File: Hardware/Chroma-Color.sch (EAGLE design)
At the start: 65 parts, among them J1 15-91-1102, J2 87832-6422, J3 1775470-6, J4 D2514-6V0C-AR-WD, J7 26-64-4040, U1 EP4CE6E22C8N, U2 ADP3338AKCZ-3.3-RL, U3 ADP3338AKCZ-2.5-RL, U4 NCV565ST12T3G, U5 M25P40-VMN6TPBCT, X1 ASDMB-50.000MHZ-LC-T

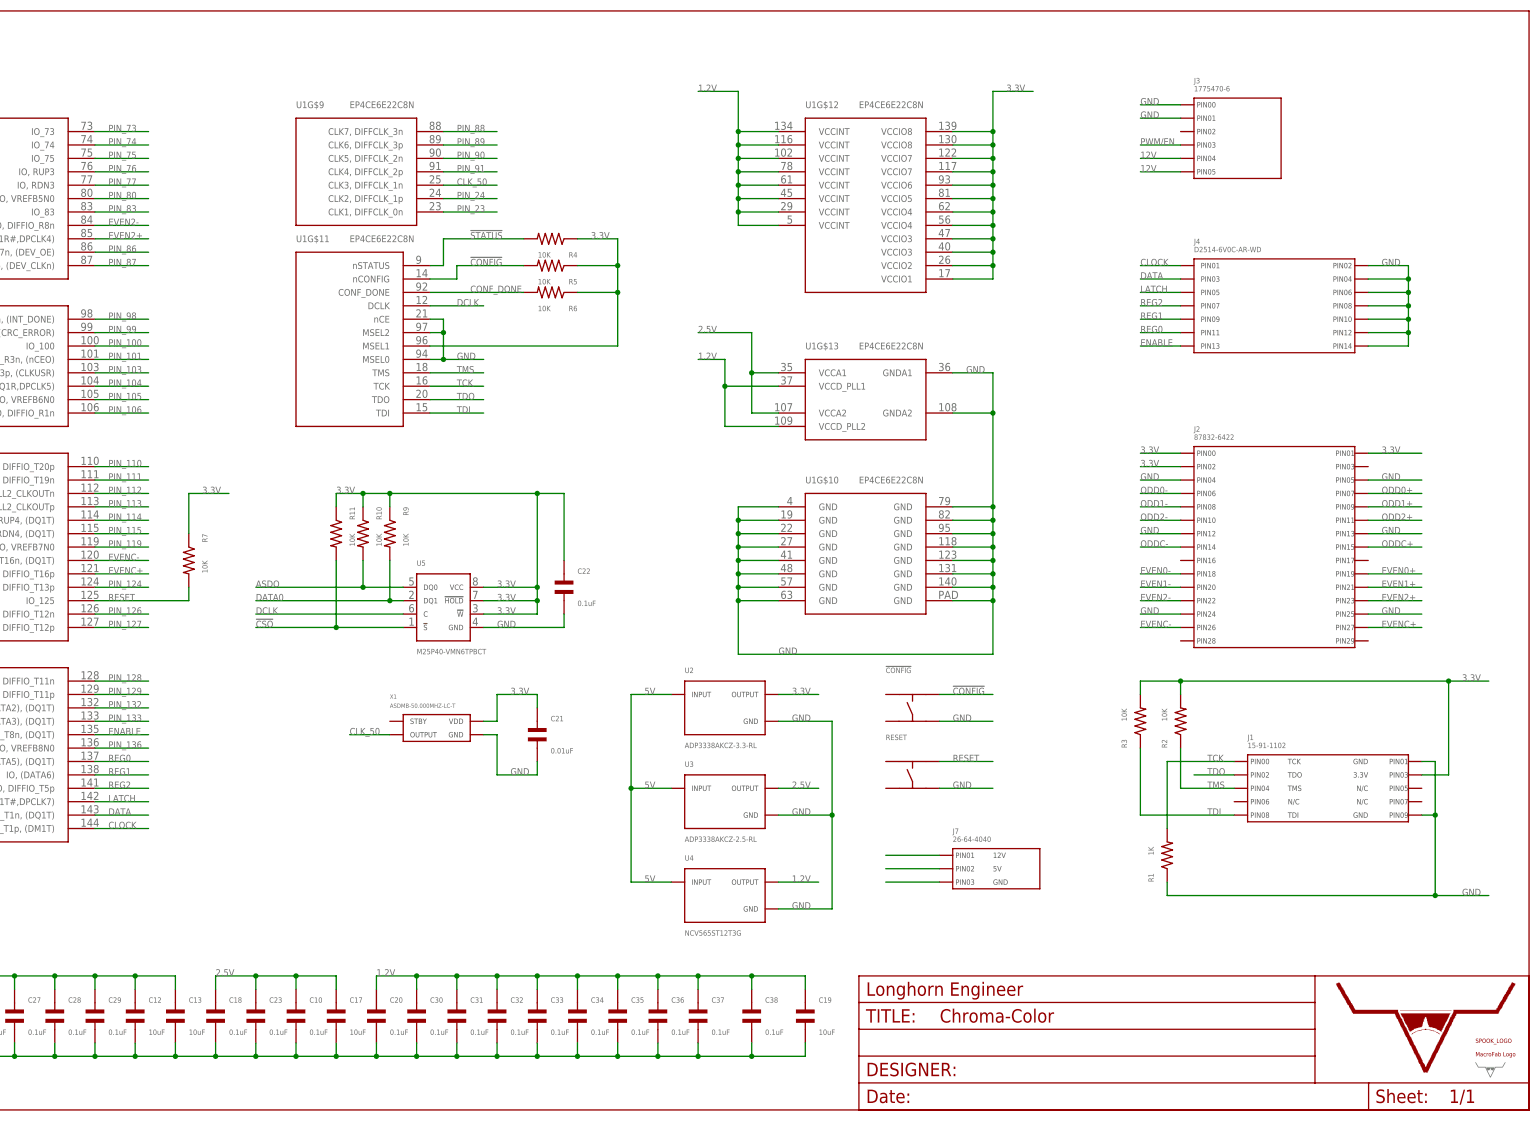
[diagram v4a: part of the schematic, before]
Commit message: Silkscreen done. Added 2SW and 2LED.
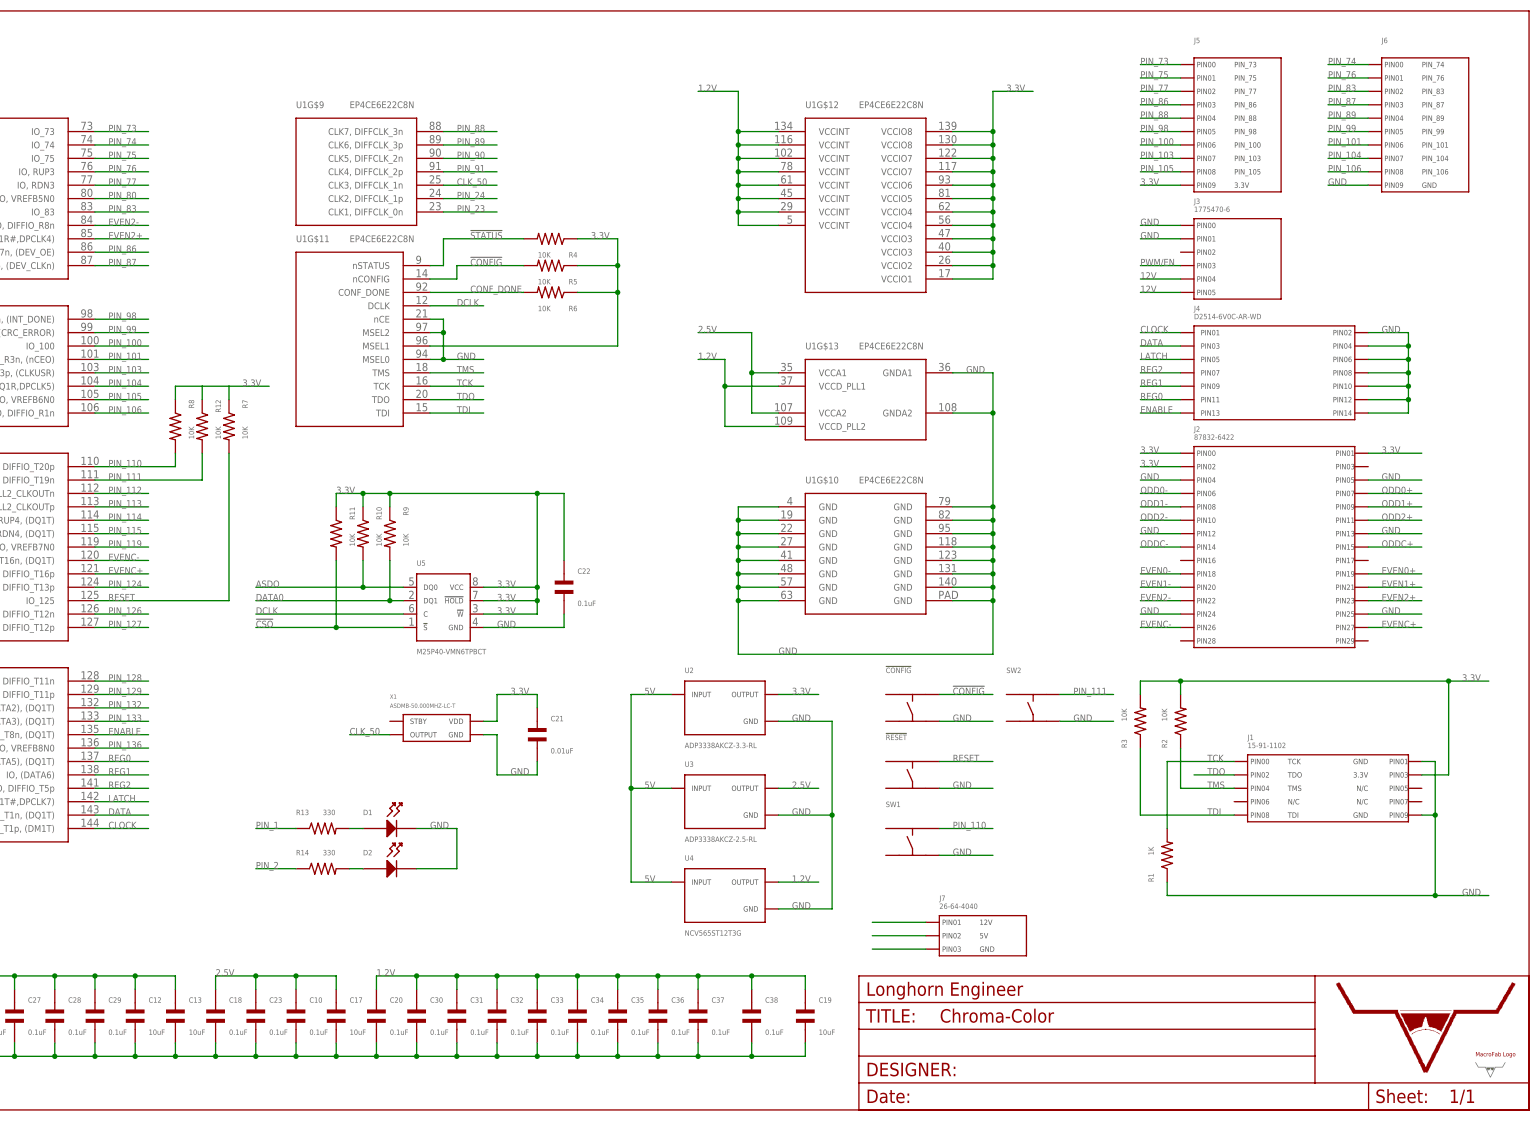
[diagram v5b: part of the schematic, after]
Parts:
- removed LOGO1: SPOOKY_LOGOSPOOKY_LOGO, PP_Aesthetics:SPOOKY_LOGOSPOOKY_LOGO
- added D1, D2: (no value), MF_LEDs:LED_SINGLE_0805
- added J5, J6: (no value), MF_Connectors:HEADER_01X10_PTH_2.54MM
- added R12, R8: 10K, MF_Passives:RESISTOR_0603
- added R13, R14: 330, MF_Passives:RESISTOR_0603
- added SW1, SW2: (no value), MF_Switches:TACT_4.2MM
- R1, R10, R11, R2, R3, R4, R5, R6, R7, R9: device MF_Passives:RESISTOR_0805 -> MF_Passives:RESISTOR_0603
- U$2: value MF_LOGOLOGO_TEXT -> MF_LOGOLOGO_MEDIUM; device PP_Aesthetics:MF_LOGOLOGO_TEXT -> PP_Aesthetics:MF_LOGOLOGO_MEDIUM
- renumbered RESET to !RESET
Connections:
- new net N$1: D1.ANODE, R13.P$2
- new net N$2: D2.ANODE, R14.P$2
- net 3.3V: now also J5.PIN9, R12.P$1, R8.P$1
- net GND: now also D1.CATHODE, D2.CATHODE, J6.PIN9, SW1.P$4, SW2.P$4
- net PIN_1: now also R13.P$1
- net PIN_100: now also J5.PIN6
- net PIN_101: now also J6.PIN6
- net PIN_103: now also J5.PIN7
- net PIN_104: now also J6.PIN7
- net PIN_105: now also J5.PIN8
- net PIN_106: now also J6.PIN8
- net PIN_110: now also R8.P$2, SW1.P$2
- net PIN_111: now also R12.P$2, SW2.P$2
- net PIN_2: now also R14.P$1
- net PIN_73: now also J5.PIN0
- net PIN_74: now also J6.PIN0
- net PIN_75: now also J5.PIN1
- net PIN_76: now also J6.PIN1
- net PIN_77: now also J5.PIN2
- net PIN_83: now also J6.PIN2
- net PIN_86: now also J5.PIN3
- net PIN_87: now also J6.PIN3
- net PIN_88: now also J5.PIN4
- net PIN_89: now also J6.PIN4
- net PIN_98: now also J5.PIN5
- net PIN_99: now also J6.PIN5
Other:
- moved on the sheet: J3, J4, J7, R7

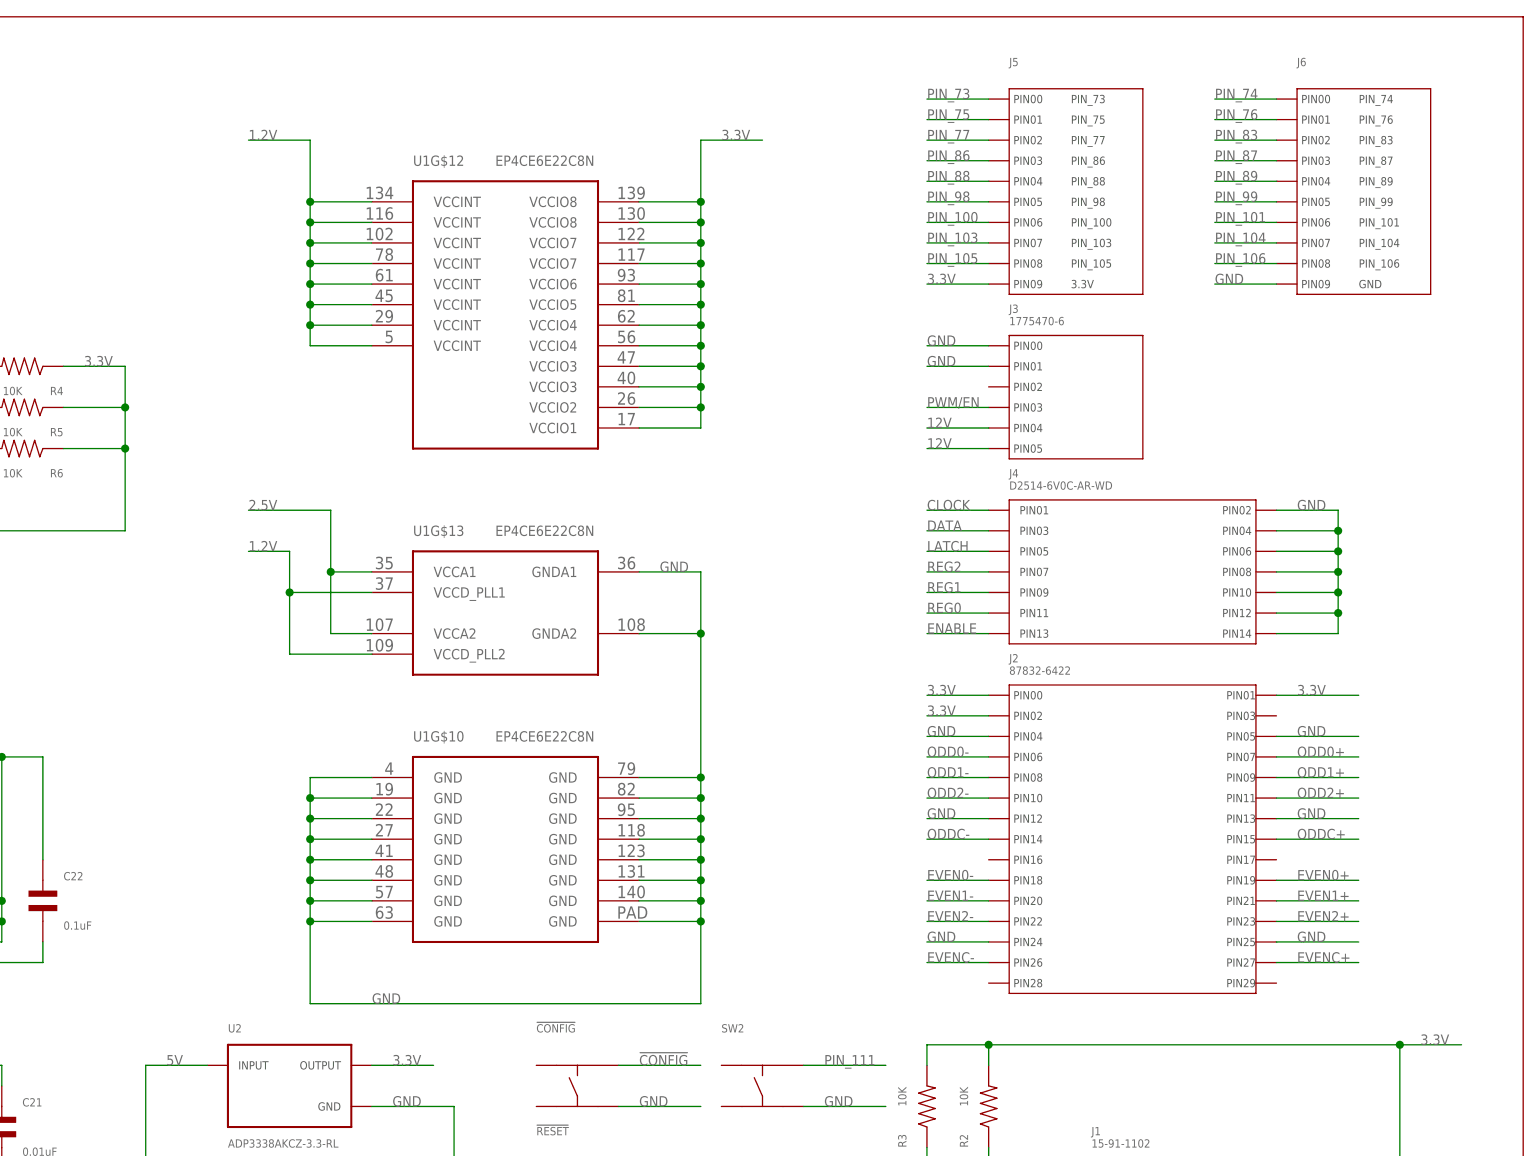
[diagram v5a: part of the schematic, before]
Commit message: Added 750ohm and 10K pulldowns on DMD con.
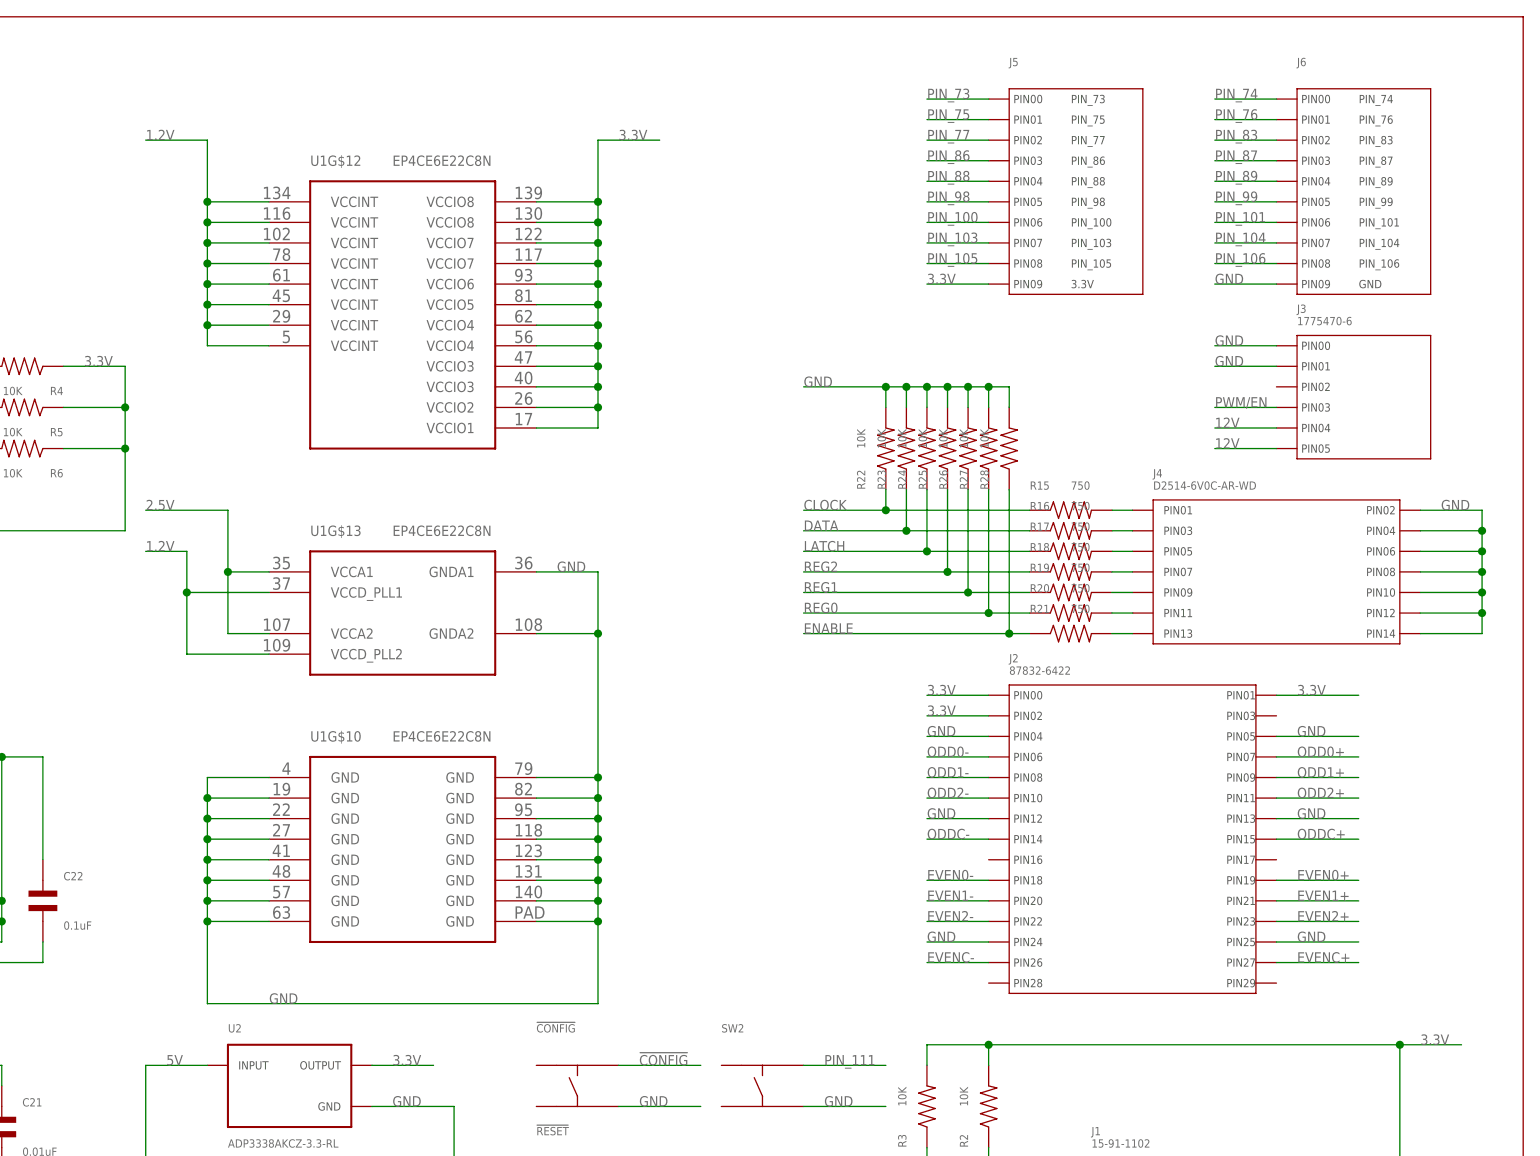
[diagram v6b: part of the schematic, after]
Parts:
- added R15, R16, R17, R18, R19, R20, R21: 750, MF_Passives:RESISTOR_0603
- added R22, R23, R24, R25, R26, R27, R28: 10K, MF_Passives:RESISTOR_0603
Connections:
- new net N$3: J4.PIN1, R15.P$2
- new net N$4: J4.PIN3, R16.P$2
- new net N$5: J4.PIN5, R17.P$2
- new net N$6: J4.PIN7, R18.P$2
- new net N$7: J4.PIN9, R19.P$2
- new net N$8: J4.PIN11, R20.P$2
- new net N$9: J4.PIN13, R21.P$2
- net CLOCK: now also R15.P$1, R22.P$1; no longer J4.PIN1
- net DATA: now also R16.P$1, R23.P$1; no longer J4.PIN3
- net ENABLE: now also R21.P$1, R28.P$1; no longer J4.PIN13
- net GND: now also R22.P$2, R23.P$2, R24.P$2, R25.P$2, R26.P$2, R27.P$2, R28.P$2
- net LATCH: now also R17.P$1, R24.P$1; no longer J4.PIN5
- net REG0: now also R20.P$1, R27.P$1; no longer J4.PIN11
- net REG1: now also R19.P$1, R26.P$1; no longer J4.PIN9
- net REG2: now also R18.P$1, R25.P$1; no longer J4.PIN7
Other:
- moved on the sheet: J3, J4, U1G$10, U1G$12, U1G$13
